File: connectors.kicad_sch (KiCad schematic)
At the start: 9 parts, among them CN102 Expansion, CN105 JOY1, CN901 HuCARD, J1 DIN-5_180degree

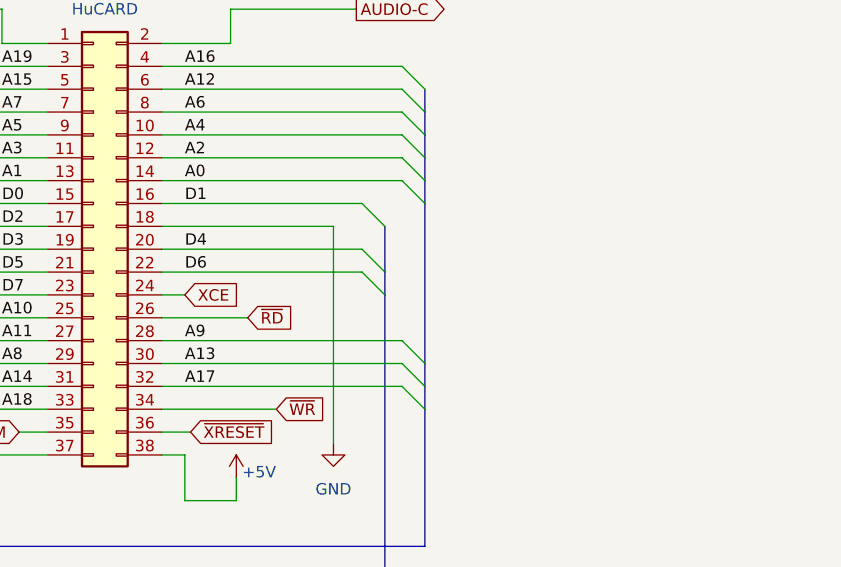
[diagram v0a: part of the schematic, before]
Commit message: Add proper scans, redo traces.
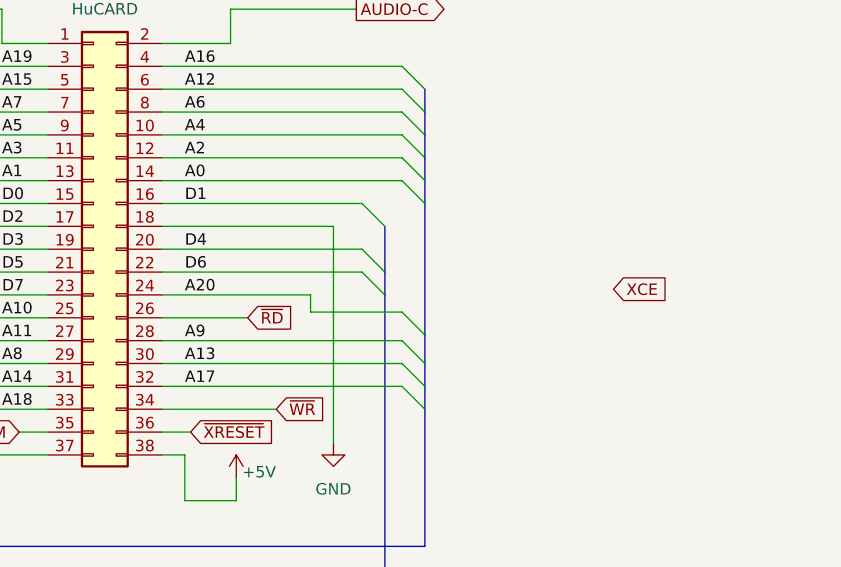
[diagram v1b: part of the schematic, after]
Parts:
- CN901: footprint Connector_PinHeader_2.54mm:PinHeader_2x19_P2.54mm_Vertical -> A-PCENGINE:Duo_HuCard
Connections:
- net A20: now also CN901.24 (Pin_24)
- net XCE: no longer CN901.24 (Pin_24)
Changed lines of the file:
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@@
+    (stroke (width 0) (type default))
+  )
+  (bus_entry (at 149.86 172.085) (size -2.54 -2.54)
     (stroke (width 0) (type default))
   )
@@
     (stroke (width 0) (type default))
   )
+  (wire (pts (xy 137.16 169.545) (xy 137.16 167.64))
+    (stroke (width 0) (type default))
+  )
   (wire (pts (xy 200.66 96.52) (xy 231.14 96.52))
     (stroke (width 0) (type default))
@@
     (stroke (width 0) (type default))
   )
+  (wire (pts (xy 147.32 169.545) (xy 137.16 169.545))
+    (stroke (width 0) (type default))
+  )
   (wire (pts (xy 287.02 64.77) (xy 287.02 41.91))
     (stroke (width 0) (type default))
@@
     (stroke (width 0) (type default))
   )
-  (wire (pts (xy 120.65 167.64) (xy 123.19 167.64))
+  (wire (pts (xy 120.65 167.64) (xy 137.16 167.64))
     (stroke (width 0) (type default))
   )
@@
     (stroke (width 0) (type default))
   )
-  (bus (pts (xy 149.86 157.48) (xy 149.86 175.26))
+  (bus (pts (xy 149.86 157.48) (xy 149.86 172.085))
     (stroke (width 0) (type default))
   )
@@
     (stroke (width 0) (type default))
   )
+  (bus (pts (xy 149.86 172.085) (xy 149.86 175.26))
+    (stroke (width 0) (type default))
+  )
   (bus (pts (xy 218.44 76.2) (xy 218.44 39.37))
     (stroke (width 0) (type default))
@@
   )
   (label "A2" (at 274.32 62.23 90) (fields_autoplaced)
+    (effects (font (size 1.27 1.27)) (justify left bottom))
+  )
+  (label "A20" (at 123.19 167.64 0) (fields_autoplaced)
     (effects (font (size 1.27 1.27)) (justify left bottom))
   )
@@
     )
   )
-  (global_label "XCE" (shape input) (at 123.19 167.64 0) (fields_autoplaced)
-    (effects (font (size 1.27 1.27)) (justify left))
-    (property "Intersheetrefs" "${INTERSHEET_REFS}" (at 129.7243 167.64 0)
+  (global_label "XCE" (shape input) (at 170.815 167.005 0) (fields_autoplaced)
+    (effects (font (size 1.27 1.27)) (justify left))
+    (property "Intersheetrefs" "${INTERSHEET_REFS}" (at 177.3493 167.005 0)
       (effects (font (size 1.27 1.27)) (justify left) hide)
     )
@@
       (effects (font (size 1.27 1.27)))
     )
-    (property "Footprint" "Connector_PinHeader_2.54mm:PinHeader_2x19_P2.54mm_Vertical" (at 113.03 162.56 0)
-      (effects (font (size 1.27 1.27)) hide)
-    )
+    (property "Footprint" "A-PCENGINE:Duo_HuCard" (at 113.03 162.56 0)
+      (effects (font (size 1.27 1.27)) hide)
+    )

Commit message: More tracing.
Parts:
- added R105: ?, Resistor_SMD:R_0805_2012Metric, symbol Device:R
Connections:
- net XCHECK is gone; now on net XCARD: CN901.1 (Pin_1)
- net +5V: now also R105.2
- net XCARD: now also R105.1
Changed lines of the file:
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@@
   (junction (at 313.69 119.38) (diameter 0) (color 0 0 0 0)
+  )
+  (junction (at 102.87 135.89) (diameter 0) (color 0 0 0 0)
   )
   (junction (at 313.69 111.76) (diameter 0) (color 0 0 0 0)
@@
     (stroke (width 0) (type default))
   )
+  (wire (pts (xy 102.87 133.35) (xy 102.87 135.89))
+    (stroke (width 0) (type default))
+  )
   (wire (pts (xy 222.25 130.81) (xy 222.25 124.46))
     (stroke (width 0) (type default))
@@
   )
   (wire (pts (xy 339.09 73.66) (xy 339.09 80.01))
+    (stroke (width 0) (type default))
+  )
+  (wire (pts (xy 102.87 123.825) (xy 102.87 125.73))
     (stroke (width 0) (type default))
   )
@@
     )
   )
+  (global_label "XCARD" (shape output) (at 87.63 135.89 180) (fields_autoplaced)
+    (effects (font (size 1.27 1.27)) (justify right))
+    (property "Intersheetrefs" "${INTERSHEET_REFS}" (at 78.5367 135.89 0)
+      (effects (font (size 1.27 1.27)) (justify right) hide)
+    )
+  )
   (global_label "~{CEK}" (shape input) (at 308.61 78.74 0) (fields_autoplaced)
     (effects (font (size 1.27 1.27)) (justify left))
@@
     (property "Intersheetrefs" "${INTERSHEET_REFS}" (at 293.0101 167.64 0)
       (effects (font (size 1.27 1.27)) (justify left) hide)
-    )
-  )
-  (global_label "XCHECK" (shape input) (at 87.63 135.89 180) (fields_autoplaced)
-    (effects (font (size 1.27 1.27)) (justify right))
-    (property "Intersheetrefs" "${INTERSHEET_REFS}" (at 77.2252 135.89 0)
-      (effects (font (size 1.27 1.27)) (justify right) hide)
     )
   )
@@
     )
   )
+  (symbol (lib_id "Device:R") (at 102.87 129.54 180) (unit 1)
+    (in_bom yes) (on_board yes) (dnp no) (fields_autoplaced)
+    (property "Reference" "R105" (at 105.41 128.27 0)
+      (effects (font (size 1.27 1.27)) (justify right))
+    )
+    (property "Value" "?" (at 105.41 130.81 0)
+      (effects (font (size 1.27 1.27)) (justify right))
+    )
+    (property "Footprint" "Resistor_SMD:R_0805_2012Metric" (at 104.648 129.54 90)
+      (effects (font (size 1.27 1.27)) hide)
+    )
+    (property "Datasheet" "~" (at 102.87 129.54 0)
+      (effects (font (size 1.27 1.27)) hide)
+    )
+    (pin "1")
+    (pin "2")
+    (instances
+      (project "PCE"
+        (path "/c1c718c6-a427-431e-a18b-e46f94ae8e09/1d91d06a-381a-4a70-bfc1-2abf4d159a91"
+          (reference "R105") (unit 1)
+        )
+        (path "/c1c718c6-a427-431e-a18b-e46f94ae8e09/f0c71640-5bc9-4afc-b5c0-657815871e51"
+          (reference "R526") (unit 1)
+        )
+        (path "/c1c718c6-a427-431e-a18b-e46f94ae8e09/f2e7b294-149a-4ec9-8398-41569f37f2ee"
+          (reference "R541") (unit 1)
+        )
+        (path "/c1c718c6-a427-431e-a18b-e46f94ae8e09/99dc3156-542f-4db3-aeb5-d38a9dd48b1b"
+          (reference "R902") (unit 1)
+        )
+      )
+    )
+  )
   (symbol (lib_id "Connector:DIN-5_180degree") (at 115.57 73.66 180) (unit 1)
     (in_bom yes) (on_board yes) (dnp no) (fields_autoplaced)
@@
         )
       )
+    )
+  )
+  (symbol (lib_id "power:+5V") (at 102.87 123.825 0) (unit 1)
+    (in_bom yes) (on_board yes) (dnp no) (fields_autoplaced)
+    (property "Reference" "#PWR026" (at 102.87 127.635 0)
+      (effects (font (size 1.27 1.27)) hide)
+    )
+    (property "Value" "+5V" (at 102.87 120.015 0)
+      (effects (font (size 1.27 1.27)))
+    )
+    (property "Footprint" "" (at 102.87 123.825 0)
+      (effects (font (size 1.27 1.27)) hide)
+    )
+    (property "Datasheet" "" (at 102.87 123.825 0)
+      (effects (font (size 1.27 1.27)) hide)
+    )
+    (pin "1")
+    (instances
+      (project "PCE"
+        (path "/c1c718c6-a427-431e-a18b-e46f94ae8e09/c78d7e8a-3e65-46f4-91f4-96eb31925bea"
+          (reference "#PWR026") (unit 1)
+        )
+        (path "/c1c718c6-a427-431e-a18b-e46f94ae8e09/ba362b1f-3cb7-4861-9385-2b05dca17551"
+          (reference "#PWR045") (unit 1)
+        )
+        (path "/c1c718c6-a427-431e-a18b-e46f94ae8e09/99dc3156-542f-4db3-aeb5-d38a9dd48b1b"
+          (reference "#PWR045") (unit 1)
+        )
+      )

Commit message: Power rails, etc.
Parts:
- removed G1, G2, G3, G4: TestPoint, A-PCENGINE:Grounding_pad, symbol Connector:TestPoint
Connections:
- no-connect marks 4 -> 0
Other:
- note removed: "Mounting hole grounding"
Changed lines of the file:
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@@
   (junction (at 86.36 200.66) (diameter 0) (color 0 0 0 0)
   )
-  (no_connect (at 111.76 232.41))
-  (no_connect (at 127 232.41))
-  (no_connect (at 119.38 232.41))
-  (no_connect (at 104.14 232.41))
   (bus_entry (at 218.44 106.68) (size -2.54 -2.54)
     (stroke (width 0) (type default))
@@
   )
   (text "Shield on underside\nconnects these pins\nto ground" (at 317.5 140.97 0)
-    (effects (font (size 1.27 1.27)) (justify left bottom))
-  )
-  (text "Mounting hole\ngrounding" (at 109.22 241.3 0)
     (effects (font (size 1.27 1.27)) (justify left bottom))
   )
@@
         (path "/c1c718c6-a427-431e-a18b-e46f94ae8e09/99dc3156-542f-4db3-aeb5-d38a9dd48b1b"
           (reference "#PWR056") (unit 1)
-        )
-      )
-    )
-  )
-  (symbol (lib_id "Connector:TestPoint") (at 104.14 232.41 0) (unit 1)
-    (in_bom yes) (on_board yes) (dnp no) (fields_autoplaced)
-    (property "Reference" "G1" (at 106.68 228.473 0)
-      (effects (font (size 1.27 1.27)) (justify left))
-    )
-    (property "Value" "TestPoint" (at 106.68 231.013 0)
-      (effects (font (size 1.27 1.27)) (justify left) hide)
-    )
-    (property "Footprint" "A-PCENGINE:Grounding_pad" (at 109.22 232.41 0)
-      (effects (font (size 1.27 1.27)) hide)
-    )
-    (property "Datasheet" "~" (at 109.22 232.41 0)
-      (effects (font (size 1.27 1.27)) hide)
-    )
-    (pin "1")
-    (instances
-      (project "PCE"
-        (path "/c1c718c6-a427-431e-a18b-e46f94ae8e09/ba362b1f-3cb7-4861-9385-2b05dca17551"
-          (reference "G1") (unit 1)
-        )
-        (path "/c1c718c6-a427-431e-a18b-e46f94ae8e09/99dc3156-542f-4db3-aeb5-d38a9dd48b1b"
-          (reference "G1") (unit 1)
         )
       )
@@
         (path "/c1c718c6-a427-431e-a18b-e46f94ae8e09/99dc3156-542f-4db3-aeb5-d38a9dd48b1b"
           (reference "CN105") (unit 1)
-        )
-      )
-    )
-  )
-  (symbol (lib_id "Connector:TestPoint") (at 127 232.41 0) (unit 1)
-    (in_bom yes) (on_board yes) (dnp no) (fields_autoplaced)
-    (property "Reference" "G4" (at 129.54 228.473 0)
-      (effects (font (size 1.27 1.27)) (justify left))
-    )
-    (property "Value" "TestPoint" (at 129.54 231.013 0)
-      (effects (font (size 1.27 1.27)) (justify left) hide)
-    )
-    (property "Footprint" "A-PCENGINE:Grounding_pad" (at 132.08 232.41 0)
-      (effects (font (size 1.27 1.27)) hide)
-    )
-    (property "Datasheet" "~" (at 132.08 232.41 0)
-      (effects (font (size 1.27 1.27)) hide)
-    )
-    (pin "1")
-    (instances
-      (project "PCE"
-        (path "/c1c718c6-a427-431e-a18b-e46f94ae8e09/ba362b1f-3cb7-4861-9385-2b05dca17551"
-          (reference "G4") (unit 1)
-        )
-        (path "/c1c718c6-a427-431e-a18b-e46f94ae8e09/99dc3156-542f-4db3-aeb5-d38a9dd48b1b"
-          (reference "G4") (unit 1)
         )
       )
@@
         )
       )
-    )
-  )
-  (symbol (lib_id "Connector:TestPoint") (at 111.76 232.41 0) (unit 1)
-    (in_bom yes) (on_board yes) (dnp no) (fields_autoplaced)
-    (property "Reference" "G2" (at 114.3 228.473 0)
-      (effects (font (size 1.27 1.27)) (justify left))
-    )
-    (property "Value" "TestPoint" (at 114.3 231.013 0)
-      (effects (font (size 1.27 1.27)) (justify left) hide)
-    )
-    (property "Footprint" "A-PCENGINE:Grounding_pad" (at 116.84 232.41 0)
-      (effects (font (size 1.27 1.27)) hide)
-    )
-    (property "Datasheet" "~" (at 116.84 232.41 0)
-      (effects (font (size 1.27 1.27)) hide)
-    )
-    (pin "1")
-    (instances
-      (project "PCE"
-        (path "/c1c718c6-a427-431e-a18b-e46f94ae8e09/ba362b1f-3cb7-4861-9385-2b05dca17551"
-          (reference "G2") (unit 1)
-        )
-        (path "/c1c718c6-a427-431e-a18b-e46f94ae8e09/99dc3156-542f-4db3-aeb5-d38a9dd48b1b"
-          (reference "G2") (unit 1)
-        )
-      )
-    )
-  )
-  (symbol (lib_id "Connector:TestPoint") (at 119.38 232.41 0) (unit 1)
-    (in_bom yes) (on_board yes) (dnp no) (fields_autoplaced)
-    (property "Reference" "G3" (at 121.92 228.473 0)
-      (effects (font (size 1.27 1.27)) (justify left))
-    )
-    (property "Value" "TestPoint" (at 121.92 231.013 0)
-      (effects (font (size 1.27 1.27)) (justify left) hide)
-    )
-    (property "Footprint" "A-PCENGINE:Grounding_pad" (at 124.46 232.41 0)
-      (effects (font (size 1.27 1.27)) hide)
-    )
-    (property "Datasheet" "~" (at 124.46 232.41 0)
-      (effects (font (size 1.27 1.27)) hide)
-    )
-    (pin "1")
-    (instances
-      (project "PCE"
-        (path "/c1c718c6-a427-431e-a18b-e46f94ae8e09/ba362b1f-3cb7-4861-9385-2b05dca17551"
-          (reference "G3") (unit 1)
-        )
-        (path "/c1c718c6-a427-431e-a18b-e46f94ae8e09/99dc3156-542f-4db3-aeb5-d38a9dd48b1b"
-          (reference "G3") (unit 1)
-        )
-      )

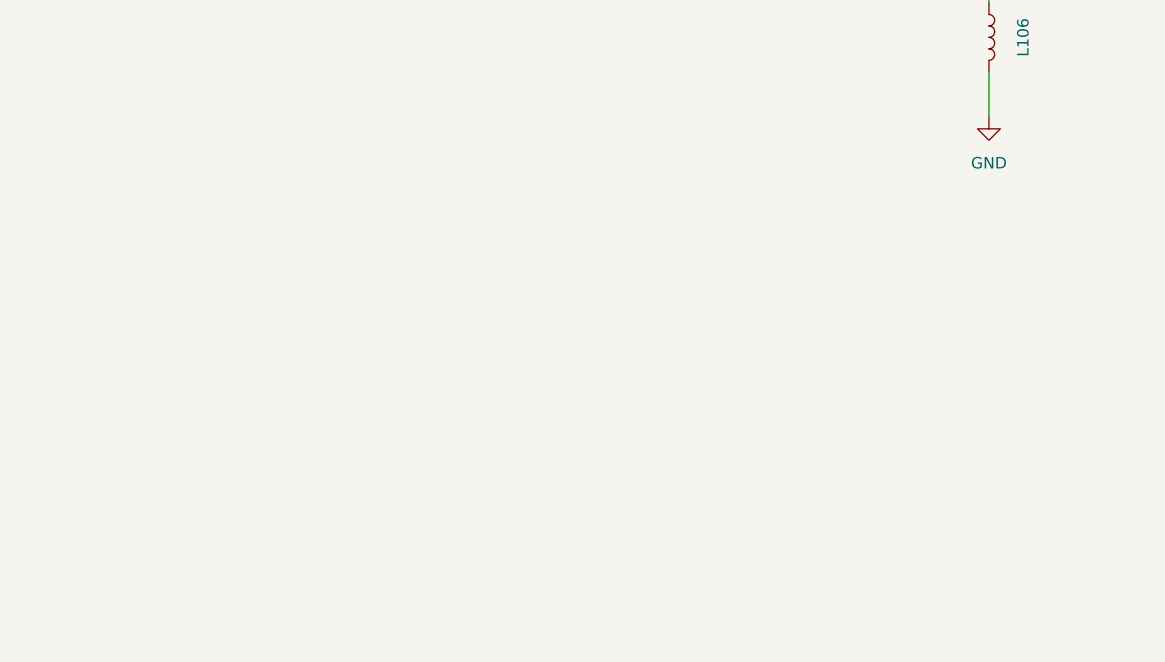
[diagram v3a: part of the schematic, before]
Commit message: IC routing mostly complete, start adding passives.
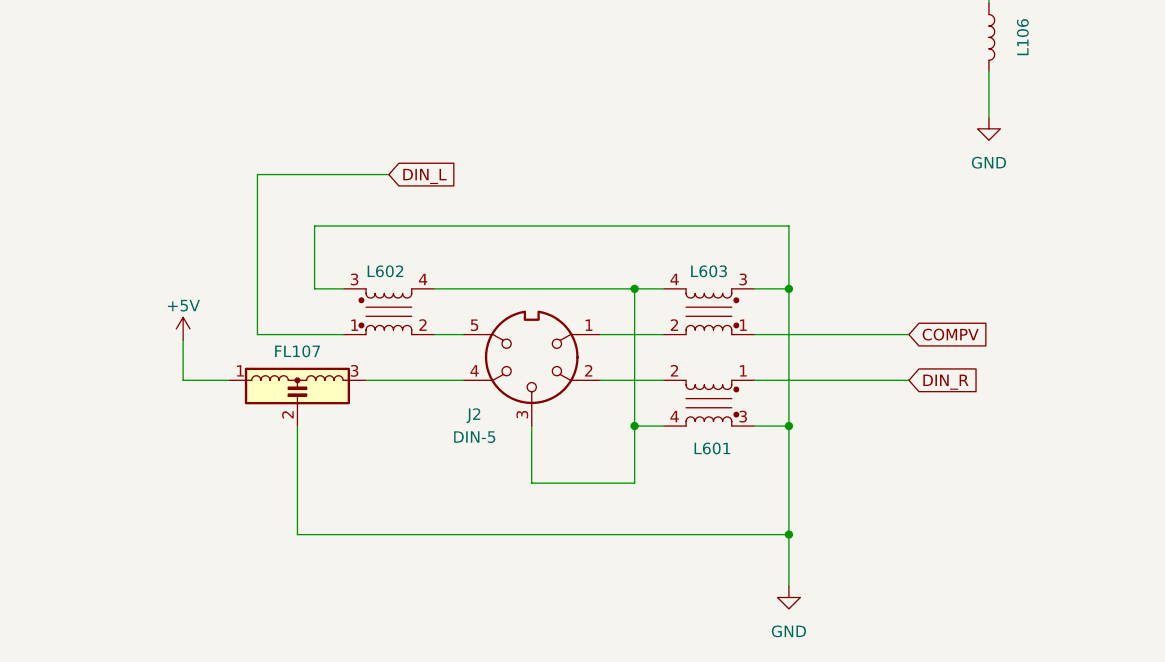
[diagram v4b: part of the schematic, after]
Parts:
- added FL107: Filter_EMI_LCL, A-PCENGINE:FL-5.00mm, symbol Device:Filter_EMI_LCL
- added J2: DIN-5, symbol Connector:DIN-5
- added L601, L602, L603: ~, A-PCENGINE:EMI_Dual_small, symbol Device:Filter_EMI_CommonMode
- R105: footprint Resistor_SMD:R_0805_2012Metric -> A-PCENGINE:SMD_0805_Narrow
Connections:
- net +5V: now also FL107.1
- net COMPV: now also L603.1
- net GND: now also FL107.2, L601.3, L602.3, L603.3
- new net: J2.2, L601.2
- new net: J2.3, L601.4, L602.4, L603.4
- new net: FL107.3, J2.4
- new net: J2.1, L603.2
- new net: J2.5, L602.2
- new net DIN_L: L602.1
- new net DIN_R: L601.1

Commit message: More passives, custom footprints, etc.
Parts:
- removed J2: DIN-5, symbol Connector:DIN-5
- added C944 (x5): N/P, A-PCENGINE:SMD_0805_Narrow_NoSilk, symbol Device:C
- added FL107: Filter_EMI_LCL, A-PCENGINE:FL-5.00mm_NoSilk, symbol Device:Filter_EMI_LCL
- added JP1, JP11, JP13, JP15, JP3, JP5, JP7, JP9: ~, A-PCENGINE:SMD_0805_Narrow_NoSilk, symbol Jumper:Jumper_2_Bridged
- added JP10, JP12, JP14, JP16, JP17, JP18, JP2, JP4, JP6, JP8: ~, A-PCENGINE:SMD_1206_C_NoSilk, symbol Jumper:Jumper_2_Bridged
- added Q304: ~, A-PCENGINE:Transistor_SMD_NoSilk, symbol Device:Q_NPN_CBE
- added TP7: B, A-PCENGINE:Test_Point_2mm_THT, symbol Connector:TestPoint
- added TP7: C, A-PCENGINE:Test_Point_2mm_THT, symbol Connector:TestPoint
- added TP7: A, A-PCENGINE:Test_Point_2mm_THT, symbol Connector:TestPoint
- JK601: renamed from J1; footprint (none) -> A-PCENGINE:DIN-5; symbol Connector:DIN-5_180degree -> PC-Engine:DIN-5
- R105: footprint A-PCENGINE:SMD_0805_Narrow -> A-PCENGINE:SMD_0805_Narrow_Long
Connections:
- net GND: now also JK601.0, C944.2, C944.2, C944.2, FL107.2, FL107.3, TP7.1, TP7.1; no longer JK601.2
- net at L601.2: now also JK601.1
- net at L601.4, L602.4, L603.4: now also JK601.2
- net at FL107.3: now also JK601.4
- net at JK601.3: now also L603.2
- net at JK601.5: now also L602.2
- new net: C944.1, C944.1, JP18.2 (B), Q304.1 (C)
- new net: C944.2, FL107.1, Q304.2 (B)
- new net: C944.1, C944.1, C944.1, Q304.3 (E)
- new net +5VD: JP18.1 (A)
- new net CFX10: JP15.1 (A), JP15.2 (B), JP16.1 (A), JP16.2 (B)
- new net CFX3: JP1.1 (A), JP1.2 (B), JP2.1 (A), JP2.2 (B)
- new net CFX4: JP3.1 (A), JP3.2 (B), JP4.1 (A), JP4.2 (B)
- new net CFX5: JP5.1 (A), JP5.2 (B), JP6.1 (A), JP6.2 (B)
- new net CFX6: JP7.1 (A), JP7.2 (B), JP8.1 (A), JP8.2 (B)
- new net CFX7: JP10.1 (A), JP10.2 (B), JP9.1 (A), JP9.2 (B)
- new net CFX8: JP11.1 (A), JP11.2 (B), JP12.1 (A), JP12.2 (B)
- new net CFX9: JP13.1 (A), JP13.2 (B), JP14.1 (A), JP14.2 (B)
- new net EXCK: JP17.1 (A), JP17.2 (B)
- no-connect marks 0 -> 2
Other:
- moved on the sheet: FL107, L601, L602, L603
